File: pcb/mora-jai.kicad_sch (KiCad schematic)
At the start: 18 parts, among them SW1 SW_Push, SW10 SW_Push, SW11 SW_Push, SW12 SW_Push, SW13 SW_Push, SW14 SW_Push, SW15 SW_Push, SW16 SW_Push, SW2 SW_Push, SW3 SW_Push, SW4 SW_Push, SW5 SW_Push, SW6 SW_Push, SW7 SW_Push, SW8 SW_Push, SW9 SW_Push, U1 CD74HC4067M, U2 XIAO-ESP32-S3-DIP

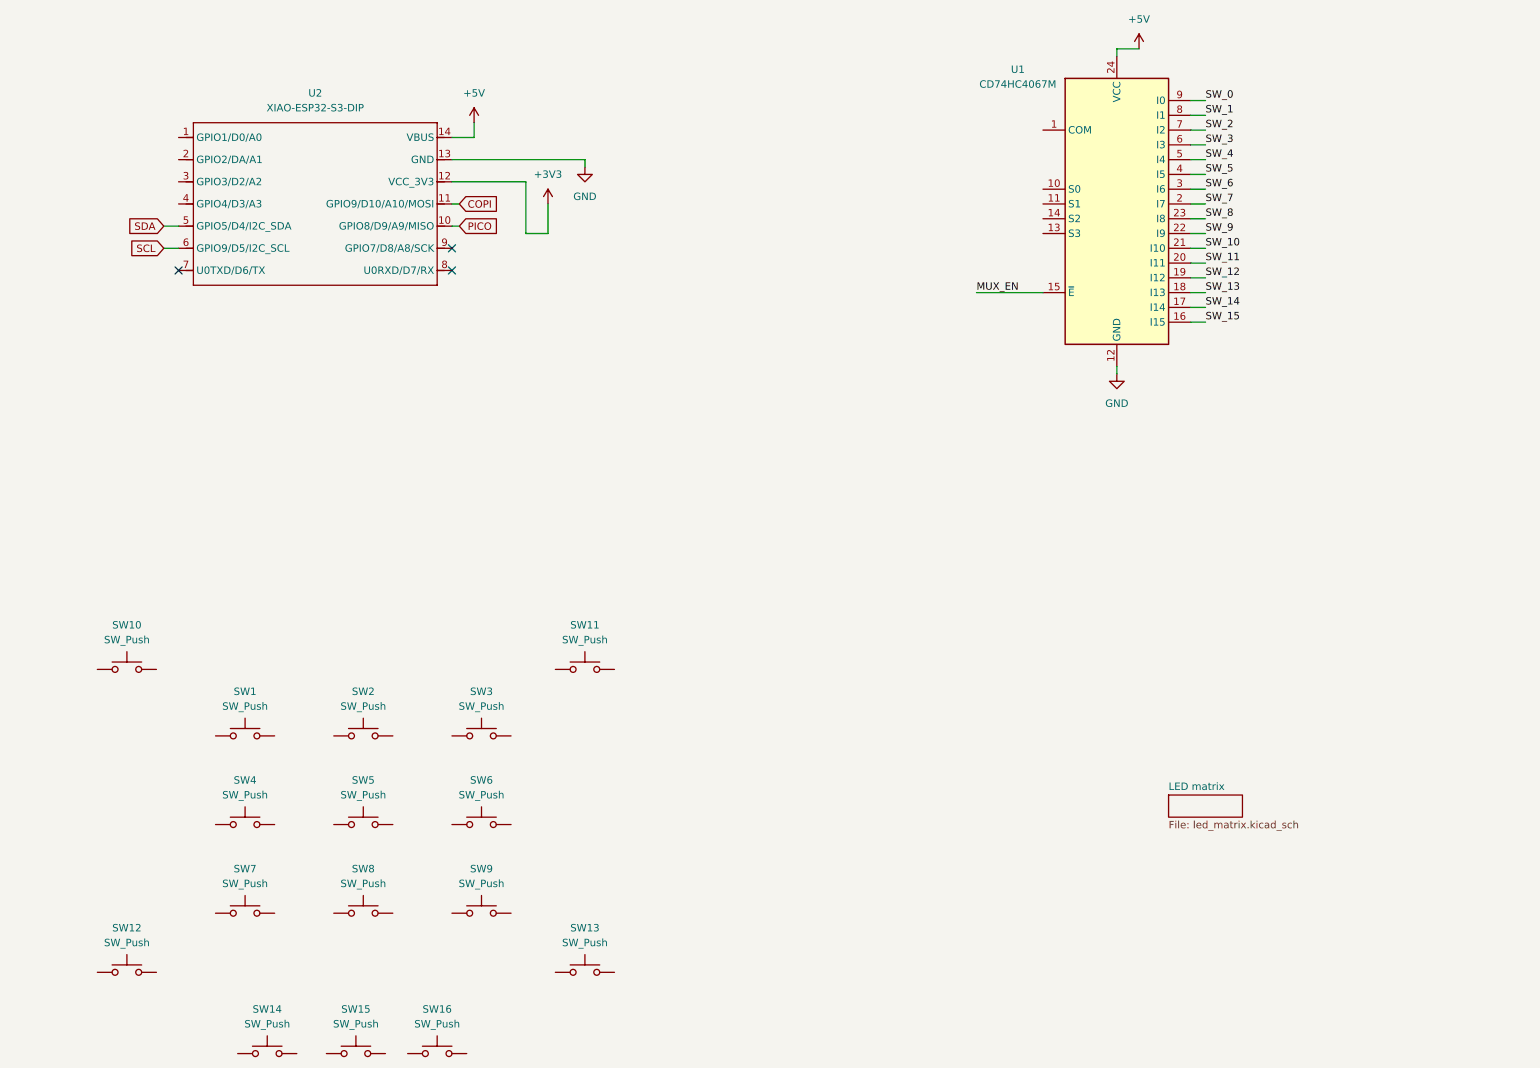
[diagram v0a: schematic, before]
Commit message: connect all components in schematic, only 13 LEDs for now
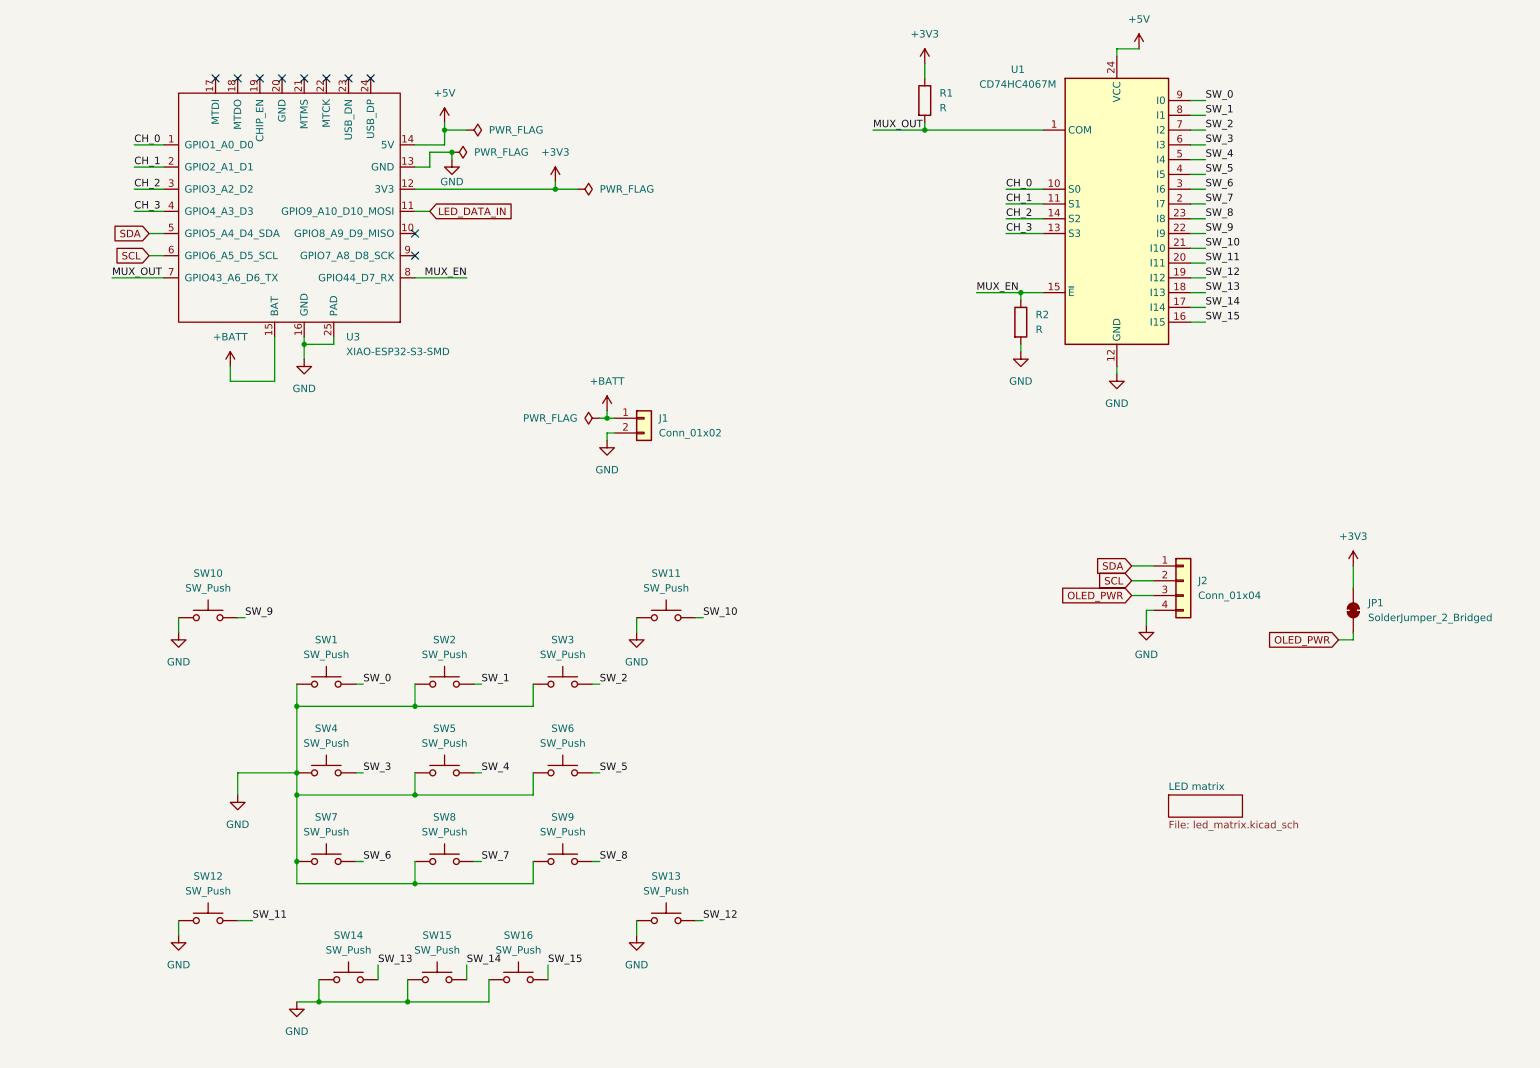
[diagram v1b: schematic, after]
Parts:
- removed U2: XIAO-ESP32-S3-DIP, Module:MOUDLE14P-XIAO-DIP-SMD, symbol Seeed_Studio_XIAO_Series:XIAO-ESP32-S3-DIP
- added J1: Conn_01x02, Connector_JST:JST_PH_S2B-PH-K_1x02_P2.00mm_Horizontal, symbol Connector_Generic:Conn_01x02
- added J2: Conn_01x04, Connector_PinSocket_2.54mm:PinSocket_1x04_P2.54mm_Vertical, symbol Connector_Generic:Conn_01x04
- added JP1: SolderJumper_2_Bridged, symbol Jumper:SolderJumper_2_Bridged
- added R1, R2: R, symbol Device:R
- added U3: XIAO-ESP32-S3-SMD, SeeedStudioXIAO:XIAO-ESP32S3-SMD, symbol Seeed_Studio_XIAO_Series:XIAO-ESP32-S3-SMD
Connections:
- net +3V3: now also JP1.2 (B), R1.1, U3.12 (3V3)
- net +5V: now also U3.14 (5V)
- net GND: now also SW1.1, SW10.1, SW11.1, SW12.1, SW13.1, SW14.1, SW15.1, SW16.1, SW2.1, SW3.1, SW4.1, SW5.1, SW6.1, SW7.1, SW8.1, SW9.1, J1.2 (Pin_2), J2.4 (Pin_4), R2.2, U3.13 (GND), U3.16 (GND), U3.25 (PAD)
- net MUX_EN: now also R2.1, U3.8 (GPIO44_D7_RX)
- net SCL: now also J2.2 (Pin_2), U3.6 (GPIO6_A5_D5_SCL)
- net SDA: now also J2.1 (Pin_1), U3.5 (GPIO5_A4_D4_SDA)
- net SW_0: now also SW1.2
- net SW_1: now also SW2.2
- net SW_10: now also SW11.2
- net SW_11: now also SW12.2
- net SW_12: now also SW13.2
- net SW_13: now also SW14.2
- net SW_14: now also SW15.2
- net SW_15: now also SW16.2
- net SW_2: now also SW3.2
- net SW_3: now also SW4.2
- net SW_4: now also SW5.2
- net SW_5: now also SW6.2
- net SW_6: now also SW7.2
- net SW_7: now also SW8.2
- net SW_8: now also SW9.2
- net SW_9: now also SW10.2
- net MUX_OUT: now reaches U1.1 (COM)
- net MUX_OUT: now also R1.2, U3.7 (GPIO43_A6_D6_TX)
- net CH_0: now reaches U1.10 (S0)
- net CH_0: now also U3.1 (GPIO1_A0_D0)
- net CH_1: now reaches U1.11 (S1)
- net CH_1: now also U3.2 (GPIO2_A1_D1)
- net CH_3: now reaches U1.13 (S3)
- net CH_3: now also U3.4 (GPIO4_A3_D3)
- net CH_2: now reaches U1.14 (S2)
- net CH_2: now also U3.3 (GPIO3_A2_D2)
- new net +BATT: J1.1 (Pin_1), U3.15 (BAT)
- new net LED_DATA_IN: U3.11 (GPIO9_A10_D10_MOSI)
- new net OLED_PWR: J2.3 (Pin_3), JP1.1 (A)
- no-connect marks 3 -> 10
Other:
- moved on the sheet: SW1, SW10, SW11, SW12, SW13, SW14, SW15, SW16, SW2, SW3, SW4, SW5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

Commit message: add description to schematic sheets
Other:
- title: (none) -> Project Mora Jai
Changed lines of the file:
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@@
 	(generator_version "9.0")
 	(paper "A4")
+	(title_block
+		(title "Project Mora Jai")
+		(date "2026-02-04")
+		(rev "1")
+		(comment 1 "CERN-OHL-S-2.0")
+	)
 	(junction
 		(at 60.96 182.88)

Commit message: start PCB dimensions
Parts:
- JP1: footprint (none) -> Jumper:SolderJumper-2_P1.3mm_Bridged_RoundedPad1.0x1.5mm
- R1, R2: footprint (none) -> Resistor_SMD:R_0805_2012Metric_Pad1.20x1.40mm_HandSolder
- SW1, SW10, SW11, SW12, SW13, SW14, SW15, SW16, SW2, SW3, SW4, SW5, SW6, SW7, SW8, SW9: footprint (none) -> Button_Switch_THT:SW_PUSH_6mm_H5mm
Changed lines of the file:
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@@
 			)
 		)
-		(property "Footprint" ""
+		(property "Footprint" "Button_Switch_THT:SW_PUSH_6mm_H5mm"
 			(at 62.23 123.19 0)
 			(effects
@@
 			)
 		)
-		(property "Footprint" ""
+		(property "Footprint" "Button_Switch_THT:SW_PUSH_6mm_H5mm"
 			(at 82.55 138.43 0)
 			(effects
@@
 			)
 		)
-		(property "Footprint" ""
+		(property "Footprint" "Button_Switch_THT:SW_PUSH_6mm_H5mm"
 			(at 41.91 163.83 0)
 			(effects
@@
 			)
 		)
-		(property "Footprint" ""
+		(property "Footprint" "Button_Switch_THT:SW_PUSH_6mm_H5mm"
 			(at 95.25 173.99 0)
 			(effects
@@
 			)
 		)
-		(property "Footprint" ""
+		(property "Footprint" "Button_Switch_THT:SW_PUSH_6mm_H5mm"
 			(at 102.87 138.43 0)
 			(effects
@@
 			)
 		)
-		(property "Footprint" ""
+		(property "Footprint" "Button_Switch_THT:SW_PUSH_6mm_H5mm"
 			(at 102.87 123.19 0)
 			(effects
@@
 			)
 		)
-		(property "Footprint" ""
+		(property "Footprint" "Resistor_SMD:R_0805_2012Metric_Pad1.20x1.40mm_HandSolder"
 			(at 163.322 27.94 90)
 			(effects
@@
 			)
 		)
-		(property "Footprint" ""
+		(property "Footprint" "Button_Switch_THT:SW_PUSH_6mm_H5mm"
 			(at 81.28 173.99 0)
 			(effects
@@
 			)
 		)
-		(property "Footprint" ""
+		(property "Footprint" "Jumper:SolderJumper-2_P1.3mm_Bridged_RoundedPad1.0x1.5mm"
 			(at 238.76 115.57 0)
 			(effects
@@
 			)
 		)
-		(property "Footprint" ""
+		(property "Footprint" "Resistor_SMD:R_0805_2012Metric_Pad1.20x1.40mm_HandSolder"
 			(at 179.832 66.04 90)
 			(effects
@@
 			)
 		)
-		(property "Footprint" ""
+		(property "Footprint" "Button_Switch_THT:SW_PUSH_6mm_H5mm"
 			(at 41.91 111.76 0)
 			(effects
@@
 			)
 		)
-		(property "Footprint" ""
+		(property "Footprint" "Button_Switch_THT:SW_PUSH_6mm_H5mm"
 			(at 62.23 138.43 0)
 			(effects
@@
 			)
 		)
-		(property "Footprint" ""
+		(property "Footprint" "Button_Switch_THT:SW_PUSH_6mm_H5mm"
 			(at 102.87 153.67 0)
 			(effects
@@
 			)
 		)
-		(property "Footprint" ""
+		(property "Footprint" "Button_Switch_THT:SW_PUSH_6mm_H5mm"
 			(at 62.23 153.67 0)
 			(effects
@@
 			)
 		)
-		(property "Footprint" ""
+		(property "Footprint" "Button_Switch_THT:SW_PUSH_6mm_H5mm"
 			(at 120.65 111.76 0)
 			(effects
@@
 			)
 		)
-		(property "Footprint" ""
+		(property "Footprint" "Button_Switch_THT:SW_PUSH_6mm_H5mm"
 			(at 82.55 123.19 0)
 			(effects
@@
 			)
 		)
-		(property "Footprint" ""
+		(property "Footprint" "Button_Switch_THT:SW_PUSH_6mm_H5mm"
 			(at 66.04 173.99 0)
 			(effects
@@
 			)
 		)
-		(property "Footprint" ""
+		(property "Footprint" "Button_Switch_THT:SW_PUSH_6mm_H5mm"
 			(at 120.65 163.83 0)
 			(effects
@@
 			)
 		)
-		(property "Footprint" ""
+		(property "Footprint" "Button_Switch_THT:SW_PUSH_6mm_H5mm"
 			(at 82.55 153.67 0)
 			(effects

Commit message: add a todo for schematic
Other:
- note added: "TODO: Add a power switch!!"
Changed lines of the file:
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@@
 		(comment 1 "CERN-OHL-S-2.0")
+	)
+	(text "TODO: Add a power switch!!"
+		(exclude_from_sim no)
+		(at 73.914 99.06 0)
+		(effects
+			(font
+				(size 5.08 5.08)
+			)
+		)
 	)
 	(junction

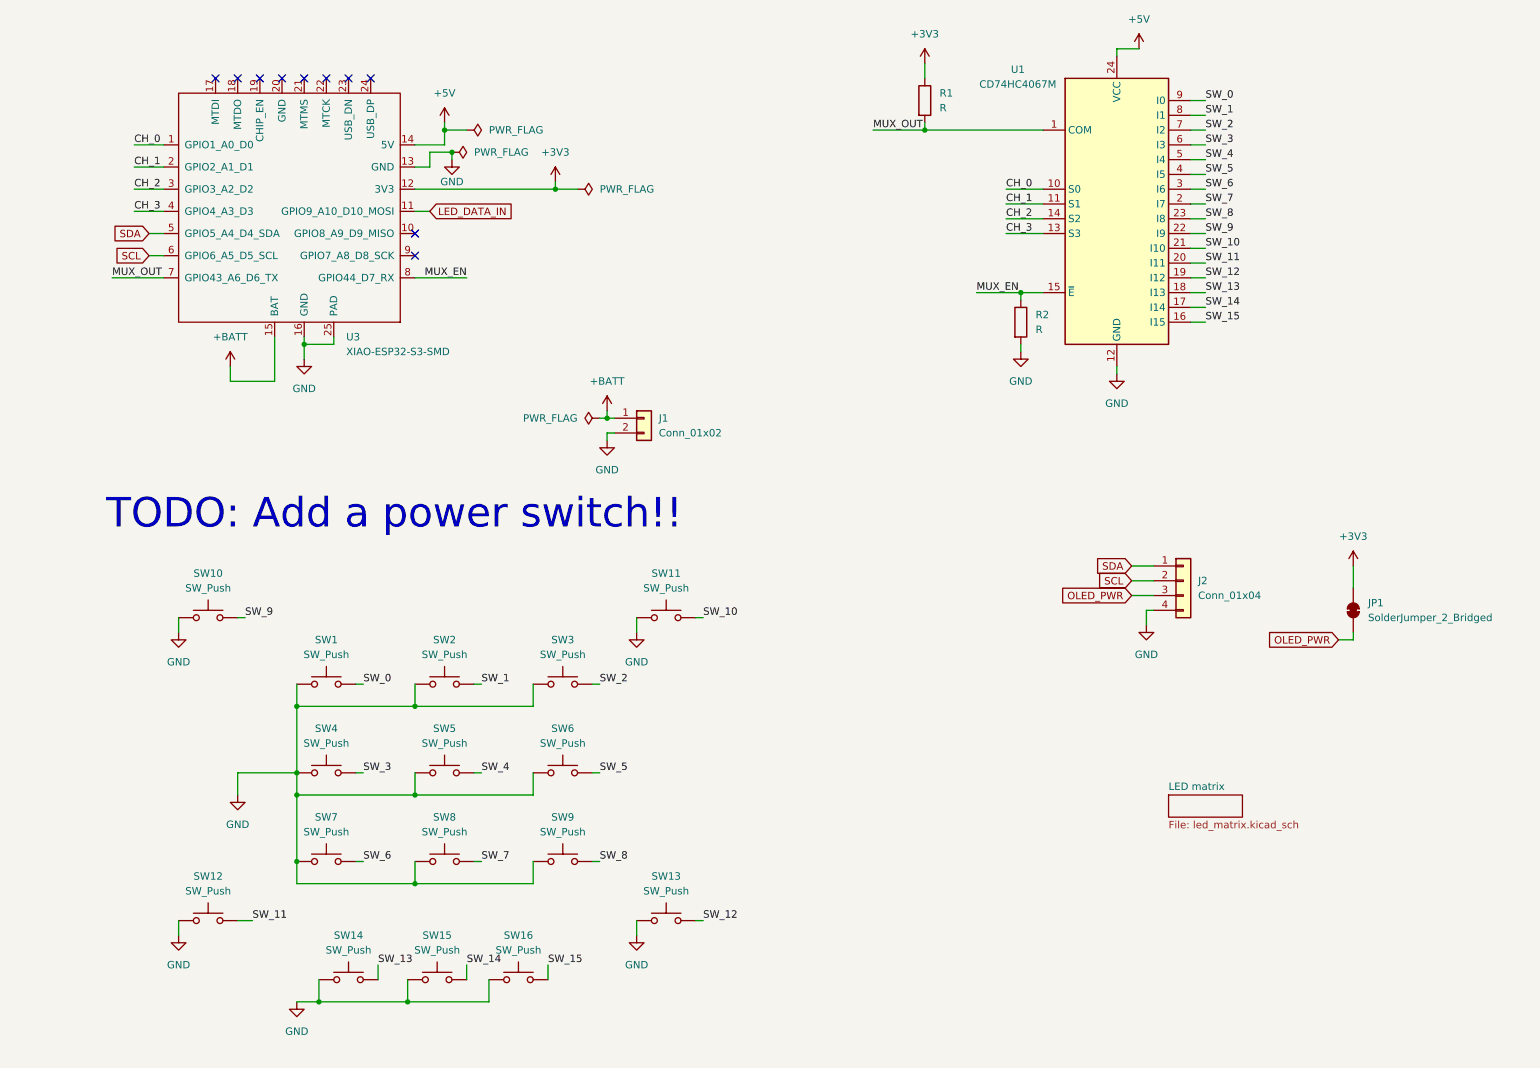
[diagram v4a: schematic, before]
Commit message: add power switch, more LEDs, and custom symbols/footprints to project
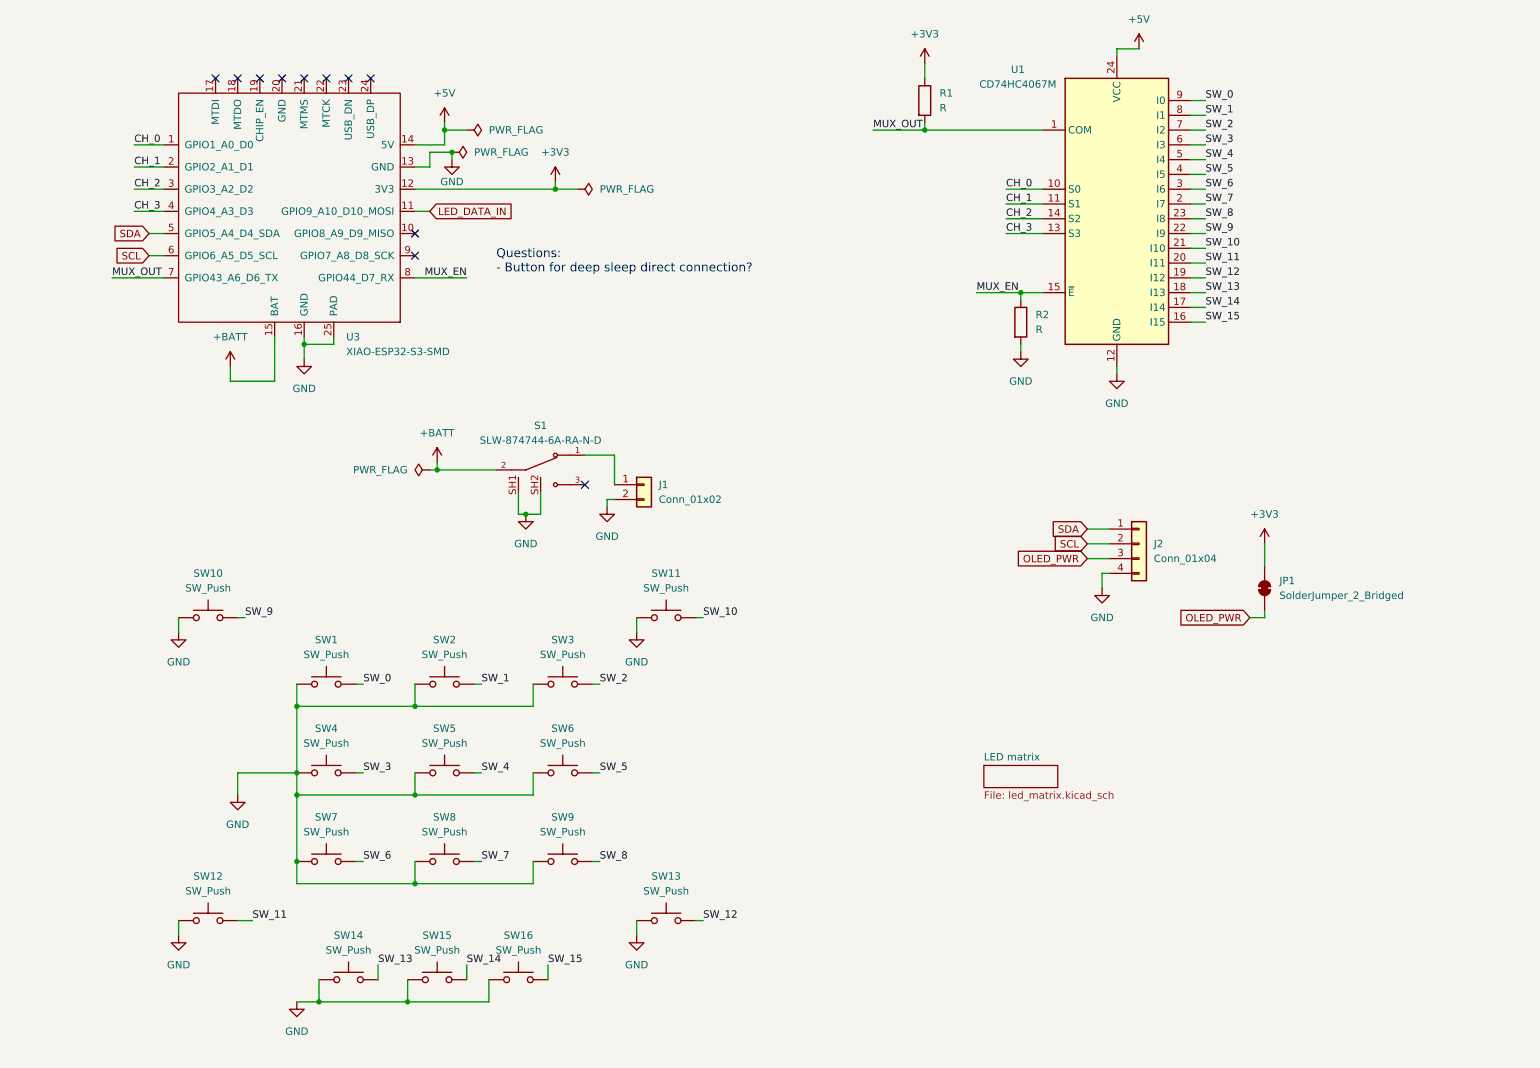
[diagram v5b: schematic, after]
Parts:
- added S1: SLW-874744-6A-RA-N-D, Mora_Jai_Parts:SW_SLW-874744-6A-RA-N-D, symbol Mora_Jai_Sym:SLW-874744-6A-RA-N-D
- U3: footprint SeeedStudioXIAO:XIAO-ESP32S3-SMD -> Mora_Jai_Parts:XIAO-ESP32S3-SMD-batt-tht
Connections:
- net +BATT: now also S1.2; no longer J1.1 (Pin_1)
- net GND: now also S1.SH1, S1.SH2
- new net: J1.1 (Pin_1), S1.1
- no-connect marks 10 -> 11
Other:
- note added: "Questions: - Button for deep sleep direct connection?"
- note removed: "TODO: Add a power switch!!"
- moved on the sheet: J1, J2, JP1

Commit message: add question
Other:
- note added: "Questions: - Button for deep sleep direct connection? - Solenoid circuit?"
- note removed: "Questions: - Button for deep sleep direct connection?"
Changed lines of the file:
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@@
 		(comment 1 "CERN-OHL-S-2.0")
 	)
-	(text "Questions:\n- Button for deep sleep direct connection?"
+	(text "Questions:\n- Button for deep sleep direct connection?\n- Solenoid circuit?"
 		(exclude_from_sim no)
 		(at 91.44 55.626 0)
